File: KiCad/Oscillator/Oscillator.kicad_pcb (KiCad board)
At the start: 2 copper layers, 150 x 130 mm, 173 parts, among them J1 691137710002, J2 691137710003, J3 691137710003, J4 691137710002, J5 691137710002, J6 691137710002, Q1 NPN, Q2 PNP, Q3 NPN, Q4 PNP, Q5 NPN, Q6 NPN, SW1 D6R90F2LFS, SW2 D6R90F2LFS, SW3 D6R90F2LFS, SW4 SW_DPST, U1 CD74HC4051E, U10 TL074, U11 TL074, U2 TL074, U3 TL074, U4 40106, U5 TL074, U6 TL074, U7 TL074, U8 TL074, U9 TL074

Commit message: oscillator pcb layout done
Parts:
- removed B1, B2: BC9VPC, Battery Holder BC9VPC:BC9VPC_MPD
- removed C10: 4u, Capacitor_THT:C_Rect_L31.5mm_W20.0mm_P27.50mm_MKS4
- removed C11, C8, C9: 1u, Capacitor_THT:C_Rect_L7.2mm_W4.5mm_P5.00mm
- removed C12, C13, C14, C15, C16, C17, C18, C19, C20, C21, C22, C23, C24, C25, C26, C27, C28, C29, C30, C31, C32, C33: 0.1u, Capacitor_SMD:C_0603_1608Metric
- removed C5: 1n, Capacitor_THT:C_Rect_L18.0mm_W5.0mm_P15.00mm_FKS3_FKP3
- removed D10, D11, D12, D13, D14, D15, D16, D17, D18, D19, D5, D6, D7, D8, D9: 1N4148, Diode_THT:D_DO-35_SOD27_P7.62mm_Horizontal
- removed J3: 691137710003, Header 691137710003:691137710003
- removed J4, J5, J6: 691137710002, Header 691137710002:691137710002
- removed Q5, Q6: NPN, Package_TO_SOT_THT:TO-92
- removed R11, R12, R21, R31, R32, R34, R35, R41, R43, R48, R49, R50, R51, R52, R53, R56, R61, R62, R67: R_US, Resistor_THT:R_Axial_DIN0207_L6.3mm_D2.5mm_P7.62mm_Horizontal
- removed R13, R15, R22, R24, R37, R38, R40, R42, R44, R45, R47, R58, R59, R64, R65, R68, R69, R70: 30k, Resistor_SMD:R_0603_1608Metric
- removed R14, R18, R20, R23, R27, R29, R30, R33, R54, R55: 100k, Resistor_SMD:R_0603_1608Metric
- removed R16, R17, R25, R26: 1M, Resistor_SMD:R_0603_1608Metric
- removed R19, R28: 2.4k, Resistor_SMD:R_0603_1608Metric
- removed R36: 10k, Resistor_SMD:R_0603_1608Metric
- removed R39, R46, R60, R66: 1k, Resistor_SMD:R_0603_1608Metric
- removed R71, R74: 15k, Resistor_SMD:R_0603_1608Metric
- removed R72, R73: 12k, Resistor_SMD:R_0603_1608Metric
- removed RV10, RV11, RV9: 100k, Potentiometer 100k PTV09A-2020F-B104:Potentiometer 100k PTV09A-2020F-B104
- removed RV12: 100k, Potentiometer_THT:Potentiometer_Bourns_3296W_Vertical
- removed RV13: 1M, Potentiometer_THT:Potentiometer_Bourns_3296W_Vertical
- removed RV14: 20k, Potentiometer_SMD:Potentiometer_Bourns_TC33X_Vertical
- removed SW1, SW2, SW3: D6R90F2LFS, Switch Push Button D6R90F2LFS:D6R90_CNK
- removed SW4: SW_DPST, DPST Switch RA83231100:DPST Switch RA83231100
- removed U10, U11, U3, U5, U6, U7, U8, U9: TL074, Package_DIP:DIP-14_W7.62mm
- removed U4: 40106, Schmitt Inv. CD40106BE:N14
- added REF**: MountingHole_3.2mm_M3, MountingHole:MountingHole_3.2mm_M3, F.Cu at (114.0, 107.0)
- added REF**: MountingHole_3.2mm_M3, MountingHole:MountingHole_3.2mm_M3, F.Cu at (44.0, 39.5)
- added REF**: MountingHole_3.2mm_M3, MountingHole:MountingHole_3.2mm_M3, F.Cu at (114.0, 39.5)
- added REF**: MountingHole_3.2mm_M3, MountingHole:MountingHole_3.2mm_M3, F.Cu at (44.0, 107.0)
- added TP10: TestPoint_Small, TestPoint:TestPoint_Keystone_5000-5004_Miniature, F.Cu at (73.0, 47.0)
- added TP11: TestPoint_Small, TestPoint:TestPoint_Keystone_5000-5004_Miniature, F.Cu at (76.0, 96.0)
- added TP20: TestPoint_Small, TestPoint:TestPoint_Keystone_5000-5004_Miniature, F.Cu at (85.0, 47.0)
- added TP4: TestPoint_Small, TestPoint:TestPoint_Keystone_5000-5004_Miniature, F.Cu at (66.0, 96.0)
- added TP6: TestPoint_Small, TestPoint:TestPoint_Keystone_5000-5004_Miniature, F.Cu at (71.0, 96.0)
- C4: value 1u -> 0.1u; footprint Capacitor_THT:C_Rect_L7.2mm_W4.5mm_P5.00mm -> Capacitor_SMD:C_0805_2012Metric
- C6, C7: value 1n -> 0.1u; footprint Capacitor_THT:C_Rect_L18.0mm_W5.0mm_P15.00mm_FKS3_FKP3 -> Capacitor_SMD:C_0805_2012Metric
- D3, D4: value 1N4148 -> LED; footprint Diode_THT:D_DO-35_SOD27_P7.62mm_Horizontal -> LED_THT:LED_D5.0mm
- J1: value 691137710002 -> Screw_Terminal_01x02
- J2: value 691137710003 -> Screw_Terminal_01x03
- R1, R4, R8: value 10k -> 100k; footprint Resistor_SMD:R_0603_1608Metric -> Resistor_SMD:R_0805_2012Metric
- R10: value 10k -> 1k; footprint Resistor_SMD:R_0603_1608Metric -> Resistor_SMD:R_0805_2012Metric
- R2, R3: value 10k -> 1M; footprint Resistor_SMD:R_0603_1608Metric -> Resistor_SMD:R_0805_2012Metric
- R5: value R_US -> 100k; footprint Resistor_THT:R_Axial_DIN0207_L6.3mm_D2.5mm_P7.62mm_Horizontal -> Resistor_SMD:R_0805_2012Metric
- R6, R7: value R_US -> 1M; footprint Resistor_THT:R_Axial_DIN0207_L6.3mm_D2.5mm_P7.62mm_Horizontal -> Resistor_SMD:R_0805_2012Metric
- R9: value R_US -> 1k; footprint Resistor_THT:R_Axial_DIN0207_L6.3mm_D2.5mm_P7.62mm_Horizontal -> Resistor_SMD:R_0805_2012Metric
- RV1, RV5, RV6: value 20k -> 100k; footprint Potentiometer_SMD:Potentiometer_Bourns_TC33X_Vertical -> Potentiometer_THT:Potentiometer_Bourns_3339P_Vertical_HandSoldering
- RV2, RV4, RV7: value 20k -> 100k; footprint Potentiometer_SMD:Potentiometer_Bourns_TC33X_Vertical -> Potentiometer_THT:Potentiometer_Bourns_PTV09A-2_Single_Horizontal
- RV3: value 20k -> 5k; footprint Potentiometer_SMD:Potentiometer_Bourns_TC33X_Vertical -> Potentiometer_THT:Potentiometer_Bourns_3339P_Vertical_HandSoldering
- RV8: value 100k -> 5k; footprint Potentiometer 100k PTV09A-2020F-B104:Potentiometer 100k PTV09A-2020F-B104 -> Potentiometer_THT:Potentiometer_Bourns_3339P_Vertical_HandSoldering
- U1: value CD74HC4051E -> 40106; footprint Mux CD74HC4051E:N16 -> Package_DIP:DIP-14_W7.62mm
- moved R3 127.6 mm to (58.5, 48.0)
- moved R1 121.4 mm to (58.5, 57.0)
- moved J1 115.9 mm to (68.5, 104.0), turned to 0 degrees
- moved RV2 115.1 mm to (59.5, 39.0), turned to 90 degrees
- moved R2 108.2 mm to (46.0, 88.0)
- moved RV3 107.1 mm to (58.5, 80.0), turned to 90 degrees
- moved RV1 106.3 mm to (61.0, 66.5), turned to 0 degrees
- moved R4 101.9 mm to (58.5, 74.0), turned to 180 degrees
- moved RV5 91.6 mm to (70.5, 52.8), turned to 90 degrees
- moved U1 89.5 mm to (75.2, 71.4)
- moved C7 88.9 mm to (85.8, 57.0)
- moved J2 87.4 mm to (84.0, 104.0), turned to 0 degrees
- moved RV4 79.9 mm to (81.5, 39.0), turned to 90 degrees
- moved C6 78.7 mm to (72.2, 58.0)
- moved RV7 73.9 mm to (103.5, 39.0), turned to 90 degrees
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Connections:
- C1 pad 1: //Oscillator/Sch Inv In 1 -> /Oscillator/Sch Inv In 1
- C2 pad 1: Net-(C2-Pad1) -> Net-(U2C--)
- C3 pad 1: //Oscillator/Sch Inv In 2 -> /Oscillator/Sch Inv In 2
- C4 pad 1: Net-(C4-Pad1) -> +9V
- C4 pad 2: Net-(U6D-+) -> GND
- C6 pad 1: GND -> +9V
- C6 pad 2: //Filter/Unprocessed Out -> GND
- C7 pad 2: Net-(D5-K) -> -9V
- D1 pad 1: //Oscillator/Sch Inv In 1 -> /Oscillator/Sch Inv In 1
- D1 pad 2: //Oscillator/Sch Inv Out 1 -> /Oscillator/Sch Inv Out 1
- D2 pad 1: //Oscillator/Sch Inv In 2 -> /Oscillator/Sch Inv In 2
- D2 pad 2: //Oscillator/Sch Inv Out 2 -> /Oscillator/Sch Inv Out 2
- D3 pad 2: //Filter/Signal In w. +Offset -> +9V
- D4 pad 1: //Filter/Unprocessed Out -> Net-(D4-K)
- D4 pad 2: Net-(D3-K) -> -9V
- J1 pad 1: //Audio Control -> /Oscillator/Control
- J1 pad 2: //Audio Out -> /Oscillator/Out
- J2 pad 1: /Custom Potentiometer Controls/Trigger 3 -> +9V
- J2 pad 2: /Custom Potentiometer Controls/Trigger 2 -> GND
- J2 pad 3: /Custom Potentiometer Controls/Trigger 1 -> -9V
- Q1 pad 1: //Oscillator/Sch Inv In 1 -> /Oscillator/Sch Inv In 1
- Q2 pad 2: //Oscillator/Core In 1 -> /Oscillator/Processed Control 1
- Q3 pad 1: //Oscillator/Sch Inv In 2 -> /Oscillator/Sch Inv In 2
- Q4 pad 2: //Oscillator/Core In 2 -> /Oscillator/Processed Control 2
- R1 pad 1: /Custom Potentiometer Controls/Pot Voltage Difference -> Net-(R1-Pad1)
- R1 pad 2: Net-(U11C--) -> Net-(R1-Pad2)
- R10 pad 1: Net-(R10-Pad1) -> Net-(D4-K)
- R10 pad 2: Net-(U3A-+) -> GND
- R2 pad 1: /Custom Potentiometer Controls/+Pot -> +9V
- R2 pad 2: Net-(U11C-+) -> Net-(Q1-B)
- R3 pad 1: Net-(U11C--) -> Net-(R3-Pad1)
- R3 pad 2: /Custom Potentiometer Controls/-Pot -> Net-(R3-Pad2)
- R4 pad 1: GND -> /Oscillator/Control
- R4 pad 2: Net-(U11C-+) -> Net-(R4-Pad2)
- R5 pad 1: Net-(U2A--) -> Net-(R5-Pad1)
- R6 pad 1: GND -> +9V
- R6 pad 2: Net-(U2A--) -> Net-(Q3-B)
- R7 pad 1: Net-(U3B-+) -> Net-(R7-Pad1)
- R7 pad 2: Net-(R10-Pad1) -> Net-(R7-Pad2)
- R8 pad 1: Net-(U3A-+) -> /Oscillator/Control
- R8 pad 2: //Filter Control -> Net-(R8-Pad2)
- R9 pad 1: //Envelope Generator/Out Filter -> Net-(D3-K)
- R9 pad 2: Net-(U3B-+) -> GND
- RV1 pad 1: +5V -> -9V
- RV1 pad 2: /Custom Potentiometer Controls/+Pot 1st Partial -> Net-(R1-Pad1)
- RV2 pad 1: +5V -> -9V
- RV2 pad 2: /Custom Potentiometer Controls/+Pot 2nd Partial -> Net-(R3-Pad1)
- RV3 pad 1: +5V -> GND
- RV3 pad 2: /Custom Potentiometer Controls/+Pot 3rd Partial -> /Oscillator/Processed Control 1
- RV3 pad 3: GND -> /Oscillator/Processed Control 1
- RV4 pad 1: +5V -> /Oscillator/Mix In 2
- RV4 pad 2: /Custom Potentiometer Controls/+Pot 4th Partial -> Net-(U2C-+)
- RV4 pad 3: GND -> /Oscillator/Mix In 1
- RV5 pad 1: +5V -> Net-(C2-Pad2)
- RV5 pad 2: /Custom Potentiometer Controls/+Pot 5th Partial -> Net-(U2B-+)
- RV6 pad 1: +5V -> GND
- RV6 pad 2: /Custom Potentiometer Controls/+Pot 6th Partial -> Net-(R5-Pad1)
- RV6 pad 3: GND -> -9V
- RV7 pad 1: +5V -> GND
- RV7 pad 2: /Custom Potentiometer Controls/+Pot 7th Partial -> Net-(R7-Pad1)
- RV7 pad 3: GND -> -9V
- RV8 pad 1: GND -> /Oscillator/Processed Control 2
- RV8 pad 2: Net-(U2D-+) -> /Oscillator/Processed Control 2
- RV8 pad 3: Net-(R5-Pad2) -> GND
- TH1 pad 1: Net-(R14-Pad2) -> Net-(R1-Pad2)
- TH1 pad 2: //Oscillator/Core In 1 -> /Oscillator/Processed Control 1
- TH2 pad 1: Net-(R17-Pad2) -> Net-(R3-Pad2)
- TH2 pad 2: //Oscillator/Core In 1 -> /Oscillator/Processed Control 1
- TH3 pad 1: Net-(R18-Pad2) -> Net-(R4-Pad2)
- TH3 pad 2: //Oscillator/Core In 1 -> /Oscillator/Processed Control 1
- TH4 pad 1: Net-(R23-Pad2) -> Net-(R5-Pad2)
- TH4 pad 2: //Oscillator/Core In 2 -> /Oscillator/Processed Control 2
- TH5 pad 1: Net-(R26-Pad2) -> Net-(R7-Pad2)
- TH5 pad 2: //Oscillator/Core In 2 -> /Oscillator/Processed Control 2
- TH6 pad 1: Net-(R27-Pad2) -> Net-(R8-Pad2)
- TH6 pad 2: //Oscillator/Core In 2 -> /Oscillator/Processed Control 2
- U1 pad 1: /Custom Potentiometer Controls/+Pot 4th Partial -> GND
- U1 pad 10: /Custom Potentiometer Controls/Trigger 2 -> unconnected-(U1-Pad10)
- U1 pad 11: /Custom Potentiometer Controls/Trigger 1 -> GND
- U1 pad 12: /Custom Potentiometer Controls/+Pot 3rd Partial -> unconnected-(U1-Pad12)
- U1 pad 14: /Custom Potentiometer Controls/+Pot 1st Partial -> +9V
- U1 pad 2: /Custom Potentiometer Controls/+Pot 6th Partial -> unconnected-(U1-Pad2)
- U1 pad 3: /Custom Potentiometer Controls/Mux Out -> GND
- U1 pad 4: /Custom Potentiometer Controls/+Pot 7th Partial -> unconnected-(U1-Pad4)
- U1 pad 5: /Custom Potentiometer Controls/+Pot 5th Partial -> /Oscillator/Sch Inv In 1
- U1 pad 6: GND -> /Oscillator/Sch Inv Out 1
- U1 pad 7: -5V -> GND
- U1 pad 8: GND -> /Oscillator/Sch Inv Out 2
- U1 pad 9: /Custom Potentiometer Controls/Trigger 3 -> /Oscillator/Sch Inv In 2
- U2 pad 1: Net-(R5-Pad2) -> /Oscillator/Mix In 1
- U2 pad 10: //Audio Control -> Net-(U2C-+)
- U2 pad 12: Net-(U2D-+) -> /Oscillator/Sch Inv In 2
- U2 pad 13: //Audio Out -> /Oscillator/Mix In 2
- U2 pad 14: //Audio Out -> /Oscillator/Mix In 2
- U2 pad 2: Net-(U2A--) -> /Oscillator/Mix In 1
- U2 pad 3: //Amplifier/Out -> /Oscillator/Sch Inv In 1
- U2 pad 5: GND -> Net-(U2B-+)
- U2 pad 6: /Power/Thaw 2 -> /Oscillator/Out
- U2 pad 7: /Power/Thaw 2 -> /Oscillator/Out
- U2 pad 8: //Buffered Audio Control -> Net-(U2C--)
- U2 pad 9: //Buffered Audio Control -> Net-(U2C--)
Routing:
- net -9V: track 743.4 -> 168.1 mm, vias 7 -> 0
- net +9V: track 418.4 -> 150.3 mm, vias 9 -> 0
- net +5V: track 196.7 -> 0.00 mm, vias 1 -> 0
- net //Buffered Audio Control: track 175.6 -> 0.00 mm, vias 3 -> 0
- net /Oscillator/Control: track 0.00 -> 103.1 mm
- net Net-(J3-Pad1): track 71.3 -> 0.00 mm
- net GND: track 74.3 -> 8.05 mm, vias 44 -> 4
- net /Oscillator/Sch Inv In 1: track 0.00 -> 61.5 mm
- net /Oscillator/Sch Inv In 2: track 0.00 -> 59.8 mm
- net Net-(B1-Pad1): track 50.4 -> 0.00 mm
- net //Filter/Signal In w. -Offset: track 46.4 -> 0.00 mm
- net Net-(J3-Pad2): track 46.3 -> 0.00 mm
- net /Oscillator/Out: track 0.00 -> 43.2 mm
- net //Oscillator/Sch Inv In 1: track 41.1 -> 0.00 mm
- net /Oscillator/Processed Control 2: track 0.00 -> 38.0 mm
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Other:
- board size 150 x 130 mm -> 78 x 75.5 mm
- board text removed: "+"
- board text removed: "-"
- board text removed: "1"
- board text removed: "2"
- board text removed: "3"
- board text removed: "Control Buttons Board"
- board text removed: "Mux"
- board text removed: "Pot Terminals Controller"

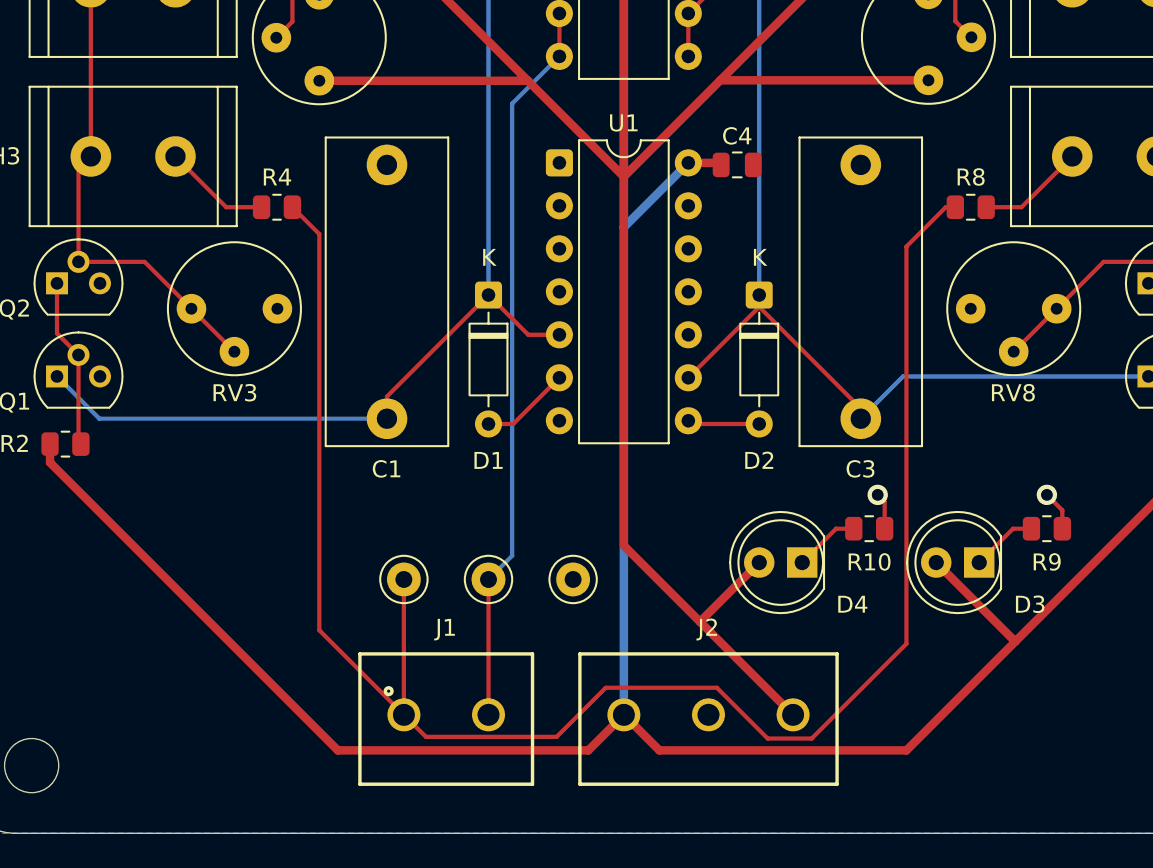
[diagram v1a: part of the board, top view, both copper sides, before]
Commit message: power pcb layout done
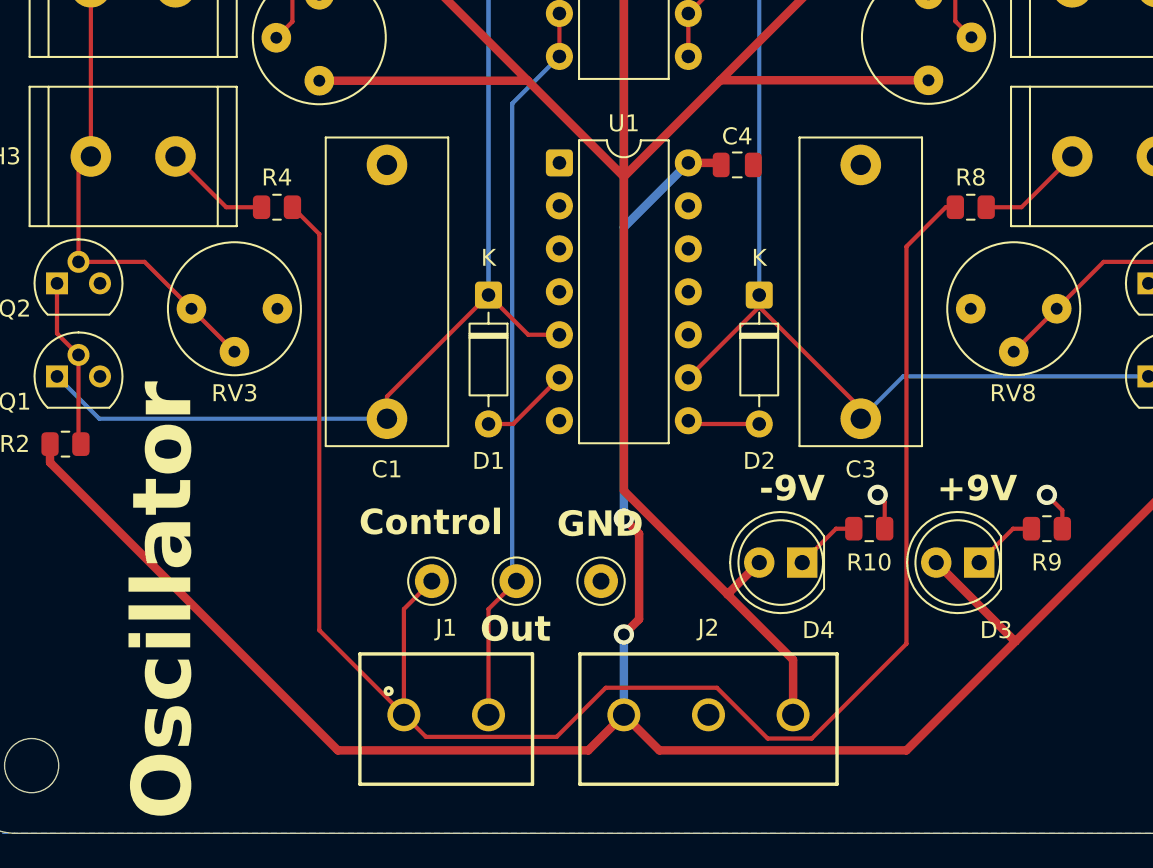
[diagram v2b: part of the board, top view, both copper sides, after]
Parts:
- moved TP11 1.65 mm to (77.7, 96.1)
- moved TP4 1.65 mm to (67.7, 96.1)
- moved TP6 1.65 mm to (72.7, 96.1)
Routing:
- net -9V: track 168.1 -> 165.8 mm
- net +9V: track 150.3 -> 151.1 mm, vias 0 -> 2
- net /Oscillator/Control: track 103.1 -> 103.6 mm
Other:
- board text added: "+9V"
- board text added: "-9V"
- board text added: "Control"
- board text added: "GND"
- board text added: "Oscillator"
- board text added: "Out"
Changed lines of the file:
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@@
 		(tags "LED")
 		(property "Reference" "D3"
-			(at -3 -2.5 0)
+			(at -1 -4 0)
 			(layer "F.SilkS")
 			(effects
@@
 	(footprint "TestPoint:TestPoint_Keystone_5000-5004_Miniature"
 		(layer "F.Cu")
-		(at 71 96)
+		(at 72.65 96.1)
 		(descr "Keystone THM Miniature Test Point 5000-5004, http://www.keyelco.com/product-pdf.cfm?p=1309")
 		(tags "Through Hole Mount Test Points")
@@
 		(tags "LED")
 		(property "Reference" "D4"
-			(at -2.96 -2.5 0)
+			(at -0.96 -4 0)
 			(layer "F.SilkS")
 			(effects
@@
 	(footprint "TestPoint:TestPoint_Keystone_5000-5004_Miniature"
 		(layer "F.Cu")
-		(at 76 96)
+		(at 77.65 96.1)
 		(descr "Keystone THM Miniature Test Point 5000-5004, http://www.keyelco.com/product-pdf.cfm?p=1309")
 		(tags "Through Hole Mount Test Points")
@@
 	(footprint "TestPoint:TestPoint_Keystone_5000-5004_Miniature"
 		(layer "F.Cu")
-		(at 66 96)
+		(at 67.65 96.1)
 		(descr "Keystone THM Miniature Test Point 5000-5004, http://www.keyelco.com/product-pdf.cfm?p=1309")
 		(tags "Through Hole Mount Test Points")
@@
 		(layer "Edge.Cuts")
 	)
+	(gr_text "-9V"
+		(at 87 91.5 0)
+		(layer "F.SilkS")
+		(effects
+			(font
+				(size 1.5 1.5)
+				(thickness 0.3)
+				(bold yes)
+			)
+			(justify left bottom)
+		)
+	)
+	(gr_text "+9V"
+		(at 97.5 91.5 0)
+		(layer "F.SilkS")
+		(effects
+			(font
+				(size 1.5 1.5)
+				(thickness 0.3)
+				(bold yes)
+			)
+			(justify left bottom)
+		)
+	)
+	(gr_text "Control"
+		(at 67.6 93.5 0)
+		(layer "F.SilkS")
+		(effects
+			(font
+				(size 1.5 1.5)
+				(thickness 0.3)
+				(bold yes)
+			)
+			(justify bottom)
+		)
+	)
+	(gr_text "Out"
+		(at 72.6 99.8 0)
+		(layer "F.SilkS")
+		(effects
+			(font
+				(size 1.5 1.5)
+				(thickness 0.3)
+				(bold yes)
+			)
+			(justify bottom)
+		)
+	)
+	(gr_text "GND"
+		(at 77.6 93.6 0)
+		(layer "F.SilkS")
+		(effects
+			(font
+				(size 1.5 1.5)
+				(thickness 0.3)
+				(bold yes)
+			)
+			(justify bottom)
+		)
+	)
+	(gr_text "Oscillator"
+		(at 53.8 110.2 90)
+		(layer "F.SilkS")
+		(effects
+			(font
+				(size 3.5 3.5)
+				(thickness 0.7)
+				(bold yes)
+			)
+			(justify left bottom)
+		)
+	)
 	(segment
 		(start 97.46 95)
@@
 	)
 	(segment
+		(start 79.9 93.3)
+		(end 79 92.4)
+		(width 0.5)
+		(layer "F.Cu")
+		(net "+9V")
+	)
+	(segment
+		(start 79.9 98.35)
+		(end 79.9 93.3)
+		(width 0.5)
+		(layer "F.Cu")
+		(net "+9V")
+	)
+	(segment
 		(start 73.230885 57.469115)
 		(end 73.2 57.5)
@@
 	)
 	(segment
+		(start 79 99.25)
+		(end 79.9 98.35)
+		(width 0.5)
+		(layer "F.Cu")
+		(net "+9V")
+	)
+	(segment
 		(start 102.15 99.65)
 		(end 112.9125 88.8875)
@@
 		(net "+9V")
 	)
+	(via
+		(at 79 99.25)
+		(size 1.2)
+		(drill 0.7)
+		(layers "F.Cu" "B.Cu")
+		(net "+9V")
+	)
+	(via
+		(at 79 92.4)
+		(size 1.2)
+		(drill 0.7)
+		(layers "F.Cu" "B.Cu")
+		(net "+9V")
+	)
 	(segment
-		(start 79 61.279116)
-		(end 75.189999 57.469115)
+		(start 79 92.4)
+		(end 79 75.19)
 		(width 0.5)
 		(layer "B.Cu")
@@
 	)
 	(segment
-		(start 79 75.19)
-		(end 79 61.279116)
+		(start 79 104)
+		(end 79 99.25)
+		(width 0.5)
+		(layer "B.Cu")
+		(net "+9V")
+	)
+	(segment
+		(start 79 61.279116)
+		(end 75.189999 57.469115)
 		(width 0.5)
 		(layer "B.Cu")
@@
 	(segment
 		(start 79 75.19)
-		(end 82.81 71.38)
+		(end 79 61.279116)
 		(width 0.5)
 		(layer "B.Cu")
@@
 	)
 	(segment
-		(start 79 104)
-		(end 79 75.19)
+		(start 79 75.19)
+		(end 82.81 71.38)
 		(width 0.5)
 		(layer "B.Cu")
@@
 	)
 	(segment
+		(start 79 90.75)
+		(end 85.125 96.875)
+		(width 0.5)
+		(layer "F.Cu")
+		(net "-9V")
+	)
+	(segment
 		(start 97 66.5)
 		(end 84.7 66.5)
@@
 	)
 	(segment
+		(start 79 72.2)
+		(end 79 90.75)
+		(width 0.5)
+		(layer "F.Cu")
+		(net "-9V")
+	)
+	(segment
 		(start 99.395 44.305)
 		(end 97.3 46.4)
@@
 	)
 	(segment
-		(start 83.5 98.5)
-		(end 79 94)
+		(start 89 100.75)
+		(end 89 104)
 		(width 0.5)
 		(layer "F.Cu")
@@
 	)
 	(segment
-		(start 89 104)
-		(end 83.5 98.5)
+		(start 85.125 96.875)
+		(end 89 100.75)
 		(width 0.5)
 		(layer "F.Cu")
@@
 	)
 	(segment
-		(start 79 94)
-		(end 79 72.2)
-		(width 0.5)
-		(layer "F.Cu")
-		(net "-9V")
-	)
-	(segment
 		(start 79 72.2)
 		(end 79 61.279114)
@@
 	)
 	(segment
-		(start 87 95)
-		(end 83.5 98.5)
+		(start 82.809999 57.469115)
+		(end 84.330885 57.469115)
 		(width 0.5)
 		(layer "F.Cu")
@@
 	)
 	(segment
-		(start 82.809999 57.469115)
-		(end 84.330885 57.469115)
+		(start 87 95)
+		(end 85.125 96.875)
 		(width 0.5)
 		(layer "F.Cu")
@@
 	)
 	(segment
+		(start 75.189999 62.549115)
+		(end 75.189999 65.089115)
+		(width 0.25)
+		(layer "F.Cu")
+		(net "/Oscillator/Out")
+	)
+	(segment
 		(start 71 104)
-		(end 71 96)
+		(end 71 97.75)
 		(width 0.25)
 		(layer "F.Cu")
@@
 	)
 	(segment
-		(start 75.189999 62.549115)
-		(end 75.189999 65.089115)
+		(start 71 97.75)
+		(end 72.65 96.1)
 		(width 0.25)
 		(layer "F.Cu")
@@
 	)
 	(segment
-		(start 72.4 94.6)
-		(end 72.4 67.879114)
+		(start 72.4 67.879114)
+		(end 75.189999 65.089115)
 		(width 0.25)
 		(layer "B.Cu")
@@
 	)
 	(segment
-		(start 71 96)
-		(end 72.4 94.6)
+		(start 72.4 95.85)
+		(end 72.4 67.879114)
 		(width 0.25)
 		(layer "B.Cu")
@@
 	)
 	(segment
-		(start 72.4 67.879114)
-		(end 75.189999 65.089115)
+		(start 72.65 96.1)
+		(end 72.4 95.85)
 		(width 0.25)
 		(layer "B.Cu")
@@
 	)
 	(segment
-		(start 66 104)
-		(end 66 96)
-		(width 0.25)
-		(layer "F.Cu")
-		(net "/Oscillator/Control")
-	)
-	(segment
 		(start 59.4125 74)
 		(end 61 75.5875)
@@
 	)
 	(segment
+		(start 66 104)
+		(end 66 97.75)
+		(width 0.25)
+		(layer "F.Cu")
+		(net "/Oscillator/Control")
+	)
+	(segment
 		(start 84.5 102.4)
 		(end 87.5 105.4)
@@
 		(width 0.25)
 		(layer "F.Cu")
+		(net "/Oscillator/Control")
+	)
+	(segment
+		(start 66 97.75)
+		(end 67.65 96.1)
+		(width 0.25)
+		(layer "F.Cu")
